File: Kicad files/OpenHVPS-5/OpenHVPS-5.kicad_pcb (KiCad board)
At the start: 2 copper layers, 40.6 x 20.8 mm, 82 parts, among them J1 Conn_01x03_Male, Q1 FQT7N10, Q2 BC846A, Q3 MMDT3906, U1 MAX6008AEUR+T, U2 74HC14, U3 MAX4162, U4 CD14538BM

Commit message: Cahnged numbering caps
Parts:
- renumbered C11 to C10, C12 to C11, C13 to C12, C14 to C13, C16 to C14, C17 to C15, C18 to C16, C20 to C17, C21 to C18, C10 to C23, C15 to C24
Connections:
- D9 pad 2: no_connect_(D9-Pad2) -> unconnected-(D9-Pad2)
- U1 pad 3: no_connect_(U1-Pad3) -> unconnected-(U1-Pad3)
- U4 pad 10: no_connect_(U4-Pad10) -> unconnected-(U4-Pad10)
- U4 pad 14: no_connect_(U4-Pad14) -> unconnected-(U4-Pad14)
- U4 pad 7: no_connect_(U4-Pad7) -> unconnected-(U4-Pad7)
- U4 pad 9: no_connect_(U4-Pad9) -> unconnected-(U4-Pad9)

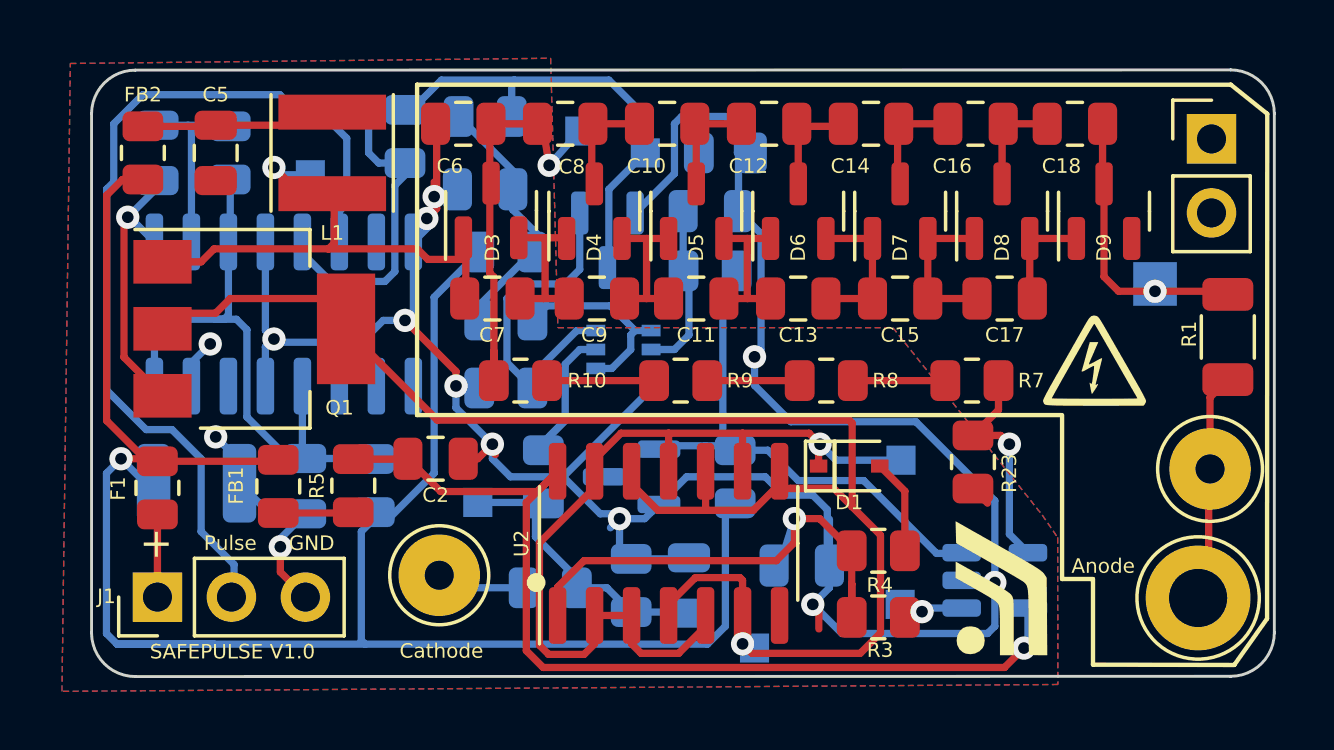
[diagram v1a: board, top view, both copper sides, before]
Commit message: fixed missing graphis and  3d model
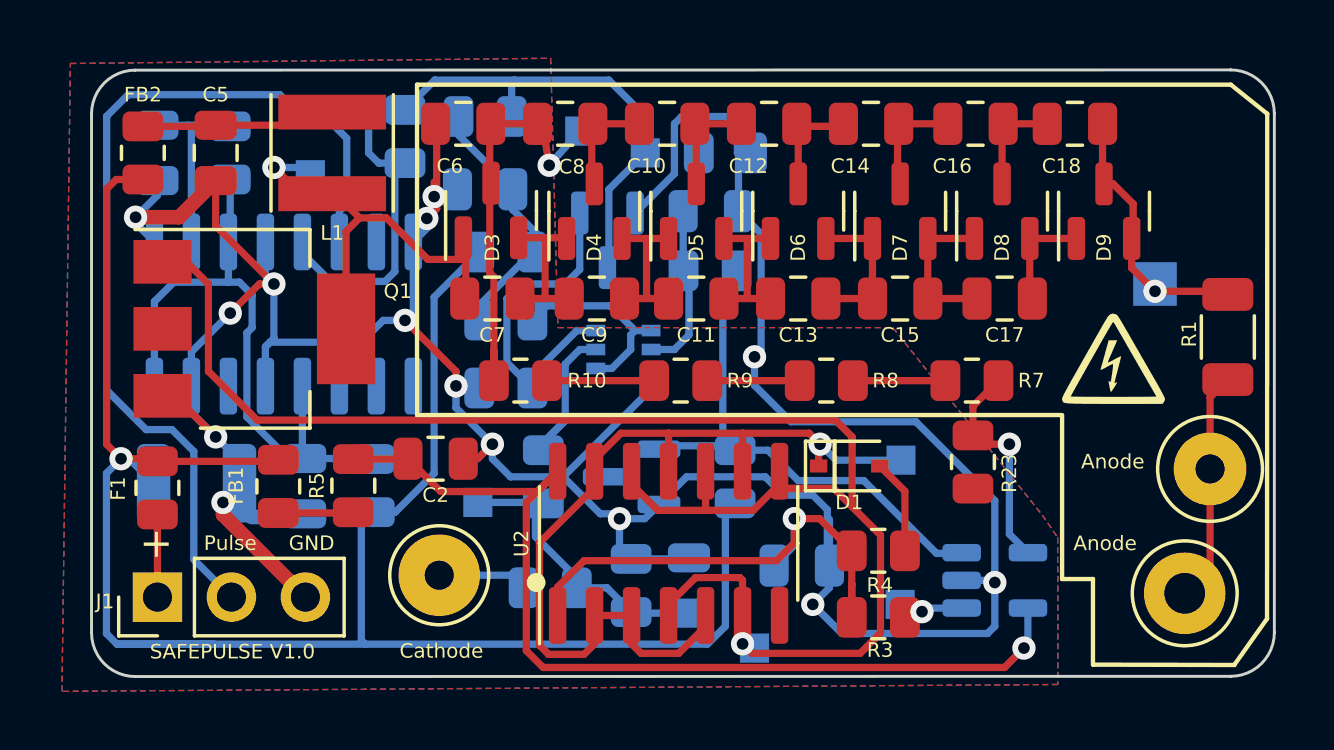
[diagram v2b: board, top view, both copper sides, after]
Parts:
- removed ?: LOGO, Symbol:QR_code_SafePulse
- removed the G*** at (157.5, 75.0)
- removed the G*** at (160.6, 67.1)
- removed the G*** at (164.5, 66.8)
- removed the H2 at (164.2, 75.3)
- removed REF**: PinHeader_1x02_P2.54mm_Vertical, Connector_PinHeader_2.54mm:PinHeader_1x02_P2.54mm_Vertical
- added G***: LOGO, Symbol:QR_code_SafePulse, F.Cu at (156.0, 64.0)
- added G2: LOGO, Symbol:HV warning, F.Cu at (161.3, 67.1)
- added G2: LOGO, Symbol:HV warning, B.Cu at (164.1, 60.2)
- added H4: Anode, TestPoint:TestPoint_Loop_D3.50mm_Drill1.4mm_Beaded, F.Cu at (163.8, 75.1)
- D3, D4, D5, D6, D7, D8, D9: value BAV23 -> BAV23S
- L1: value 2.2uH -> 4.7uH
- Q1: footprint Package_TO_SOT_SMD:SOT-223-3_TabPin2 -> Package_TO_SOT_SMD:SOT-223-3_TabPin4
- R1: value 10M -> 4.7M
- R20: value 560K -> 470K
- R4: value 100K -> 10K
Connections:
- D9 pad 2: unconnected-(D9-Pad2) -> Net-(C18-Pad2)
- Q1 pad 1: Net-(C7-Pad1) -> Net-(Q1-Pad1)
- TP4 pad 1: Net-(Q1-Pad2) -> Net-(Q1-Pad1)
- U2 pad 10: Net-(Q1-Pad2) -> Net-(Q1-Pad1)
- U2 pad 12: Net-(Q1-Pad2) -> Net-(Q1-Pad1)
- U2 pad 4: Net-(Q1-Pad2) -> Net-(Q1-Pad1)
- U2 pad 6: Net-(Q1-Pad2) -> Net-(Q1-Pad1)
- U2 pad 8: Net-(Q1-Pad2) -> Net-(Q1-Pad1)
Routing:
- net Net-(Q1-Pad1): track 0.00 -> 58.2 mm, vias 0 -> 1
- net Net-(Q1-Pad2): track 57.4 -> 0.00 mm, vias 1 -> 0
- net GND: track 117.9 -> 125.8 mm
- net Net-(C7-Pad1): track 19.3 -> 17.2 mm
- net +3V3: track 71.6 -> 70.2 mm
- net Net-(C23-Pad1): track 21.3 -> 22.5 mm
- net Net-(R3-Pad2): track 2.08 -> 1.41 mm
- net Net-(H1-Pad1): track 3.61 -> 3.08 mm
- net Net-(C18-Pad2): track 10.5 -> 9.94 mm
- net Net-(H2-Pad1): track 8.74 -> 9.25 mm

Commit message: Updated the board to V1.1.
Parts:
- removed TP7: TestPoint, TestPoint:TestPoint_Pad_1.5x1.5mm
- added two_pinheader1: Conn_01x03_Male, Connector_PinHeader_2.54mm:PinHeader_1x02_P2.54mm_Vertical, F.Cu at (165.1, 59.1)
- moved G2 7.50 mm to (164.2, 67.7)
- moved H2 2.27 mm to (162.6, 71.8)
- moved H4 1.29 mm to (162.6, 75.6)
- moved H1 1.06 mm to (138.2, 75.6)
- moved J1 0.31 mm to (128.5, 75.6)
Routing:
- net +3V3: track 70.2 -> 68.2 mm
- net Net-(C18-Pad2): vias 1 -> 0
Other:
- board text added: "SAFEPULSE V1.1"
- board text removed: "SAFEPULSE V1.0"

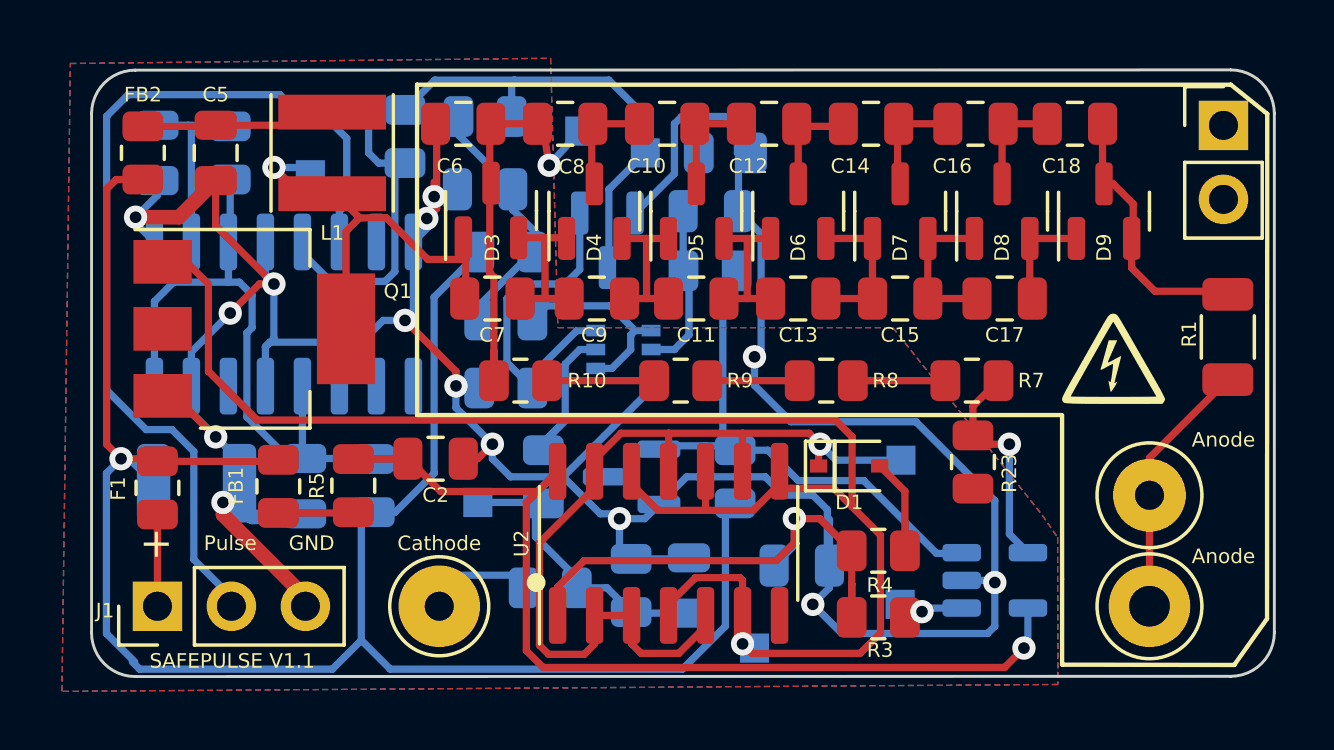
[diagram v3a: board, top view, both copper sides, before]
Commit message: Aligned more graphics and removed some via's
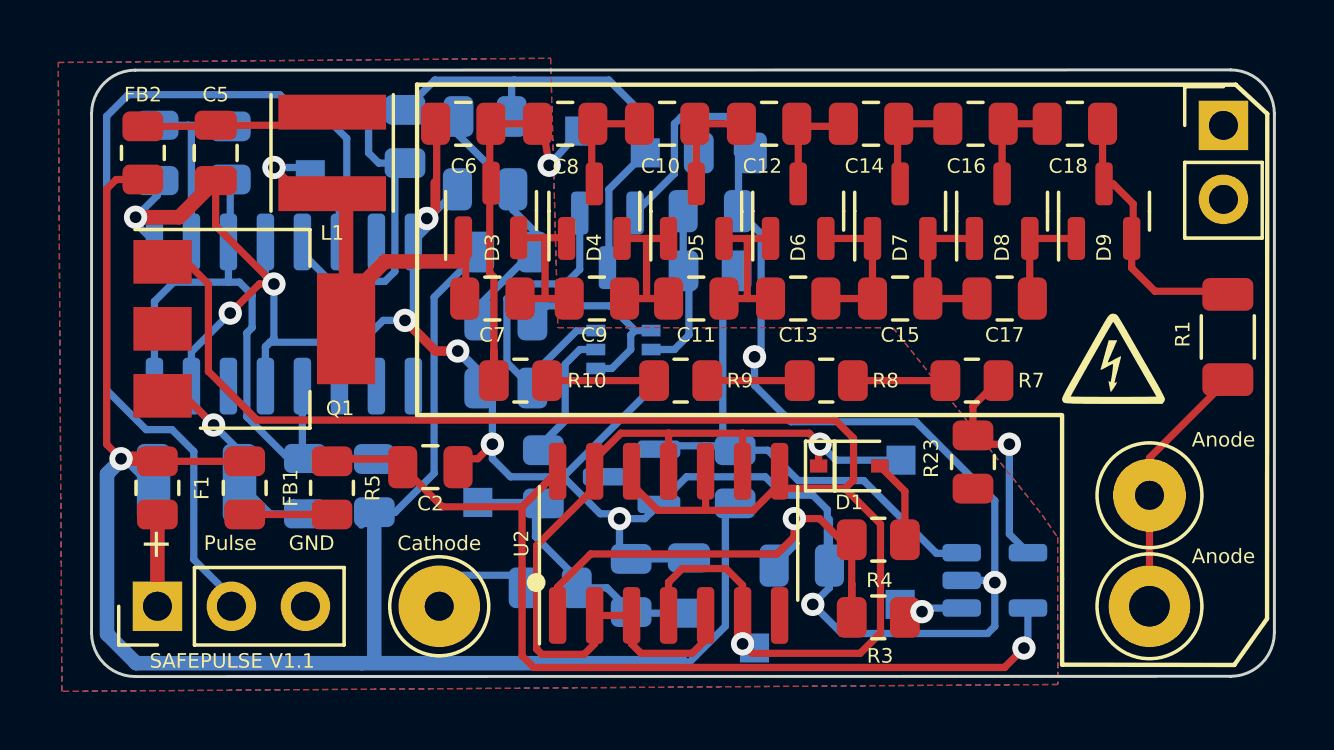
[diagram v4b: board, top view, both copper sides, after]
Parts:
- moved FB1 1.15 mm to (131.5, 71.5)
- moved R5 0.74 mm to (134.5, 71.5)
- moved R4 0.38 mm to (153.2, 73.3)
- moved C2 0.34 mm to (137.9, 70.8)
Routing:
- net Net-(C7-Pad1): track 17.2 -> 19.2 mm
- net GND: track 125.8 -> 124.4 mm, vias 14 -> 12
- net +3V3: track 68.2 -> 67.0 mm
- net Net-(Q1-Pad1): track 58.2 -> 59.4 mm

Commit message: updated board fixed via's DRC error.
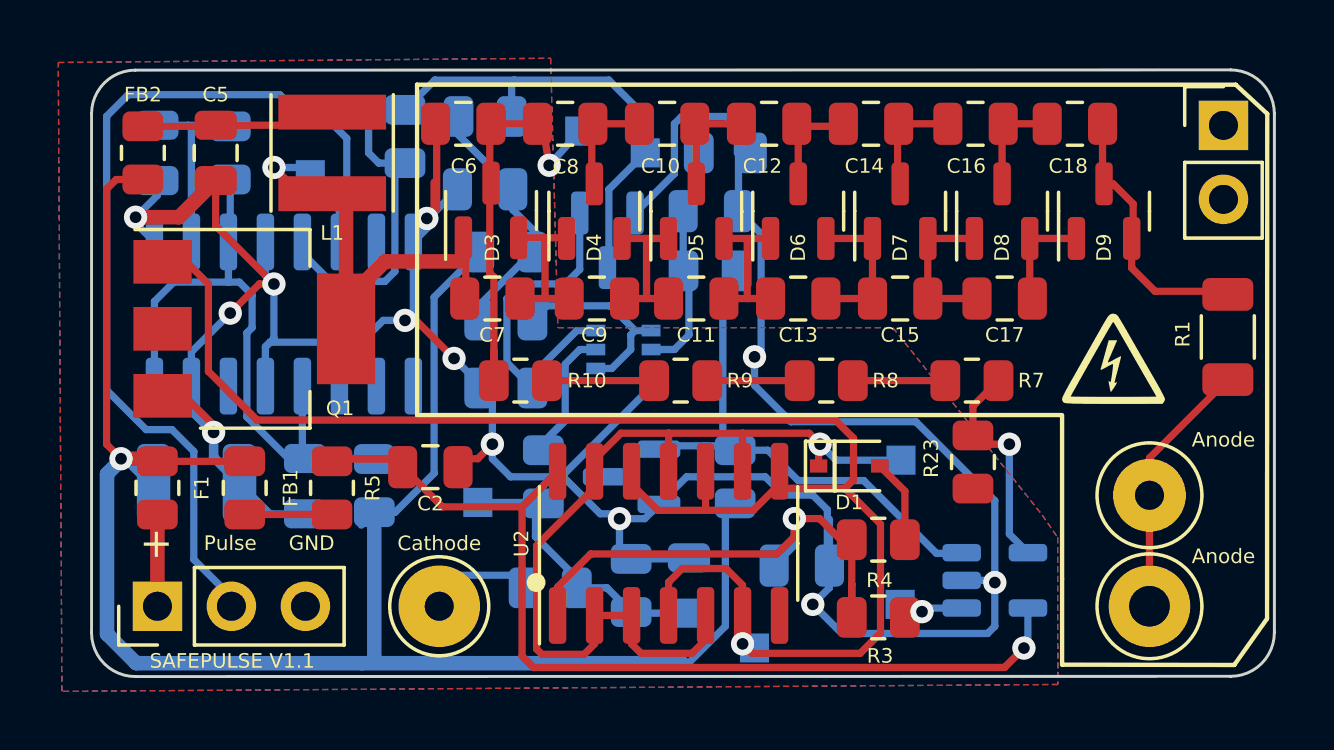
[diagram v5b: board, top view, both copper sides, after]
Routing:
- net GND: track 124.4 -> 126.5 mm
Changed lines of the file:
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@@
   (segment (start 129.242 62.208) (end 130.5 60.95) (width 0.5) (layer "F.Cu") (net 3))
   (segment (start 128.676 68.34) (end 129.09 68.34) (width 0.25) (layer "F.Cu") (net 3))
+  (segment (start 137.378 65.75) (end 138.684 67.056) (width 0.25) (layer "F.Cu") (net 3))
   (segment (start 128.676 68.34) (end 129.046 68.34) (width 0.25) (layer "F.Cu") (net 3))
   (segment (start 129.427 68.34) (end 130.429 69.342) (width 0.25) (layer "F.Cu") (net 3))
   (segment (start 127.75 62.208) (end 127.481 62.208) (width 0.25) (layer "F.Cu") (net 3))
   (segment (start 138.0875 61.9125) (end 138.0875 59) (width 0.25) (layer "F.Cu") (net 3))
-  (segment (start 138.811 66.802) (end 138.052 66.802) (width 0.3302) (layer "F.Cu") (net 3))
+  (segment (start 137 65.75) (end 137.378 65.75) (width 0.25) (layer "F.Cu") (net 3))
   (segment (start 138 62) (end 138 61) (width 0.25) (layer "F.Cu") (net 3))
-  (segment (start 138.052 66.802) (end 137 65.75) (width 0.3302) (layer "F.Cu") (net 3))
   (segment (start 137.75 62.25) (end 138 62) (width 0.25) (layer "F.Cu") (net 3))
   (segment (start 131 65.5) (end 132 64.5) (width 0.25) (layer "F.Cu") (net 3))
@@
   (via (at 132.5 64.5) (size 0.8) (drill 0.4) (layers "F.Cu" "B.Cu") (net 3))
   (via (at 127.75 62.208) (size 0.8) (drill 0.4) (layers "F.Cu" "B.Cu") (net 3))
-  (via (at 138.811 66.802) (size 0.8) (drill 0.4) (layers "F.Cu" "B.Cu") (free) (net 3))
+  (via (at 138.684 67.056) (size 0.8) (drill 0.4) (layers "F.Cu" "B.Cu") (free) (net 3))
   (via (at 157.25 74.75) (size 0.8) (drill 0.4) (layers "F.Cu" "B.Cu") (net 3))
   (via (at 131 65.5) (size 0.8) (drill 0.4) (layers "F.Cu" "B.Cu") (net 3))
@@
   (via (at 137.75 62.25) (size 0.8) (drill 0.4) (layers "F.Cu" "B.Cu") (net 3))
   (via (at 151 75.5) (size 0.8) (drill 0.4) (layers "F.Cu" "B.Cu") (net 3))
-  (via (at 130.429 69.342) (size 0.8) (drill 0.4) (layers "F.Cu" "B.Cu") (free) (net 3))
+  (via (at 130.429 69.596) (size 0.8) (drill 0.4) (layers "F.Cu" "B.Cu") (free) (net 3))
   (via (at 144.365 72.5578) (size 0.8) (layers "F.Cu" "B.Cu") (net 3))
   (via (at 137 65.75) (size 0.8) (drill 0.4) (layers "F.Cu" "B.Cu") (free) (net 3))
@@
   (segment (start 134.747 67.5418) (end 134.747 68.007) (width 0.25) (layer "B.Cu") (net 3))
   (segment (start 132.3677 66.5) (end 134.1026 66.5) (width 0.25) (layer "B.Cu") (net 3))
+  (segment (start 130.429 69.596) (end 130.429 70.4525) (width 0.3302) (layer "B.Cu") (net 3))
+  (segment (start 129.667 68.834) (end 129.667 68.007) (width 0.3302) (layer "B.Cu") (net 3))
   (segment (start 137.832 62.5121) (end 137.287 63.057) (width 0.25) (layer "B.Cu") (net 3))
+  (segment (start 130.429 69.596) (end 129.667 68.834) (width 0.3302) (layer "B.Cu") (net 3))
   (segment (start 131.318 70.568) (end 131.318 71.3415) (width 0.25) (layer "B.Cu") (net 3))
   (segment (start 127.75 62.208) (end 128.5 61.458) (width 0.25) (layer "B.Cu") (net 3))
@@
   (segment (start 148.45 62) (end 149.22502 62.77502) (width 0.25) (layer "B.Cu") (net 3))
   (segment (start 151 75.5) (end 151.572 74.928) (width 0.25) (layer "B.Cu") (net 3))
-  (segment (start 139.5495 67.5405) (end 138.811 66.802) (width 0.3302) (layer "B.Cu") (net 3))
   (segment (start 149.22502 62.77502) (end 149.22502 66.77498) (width 0.25) (layer "B.Cu") (net 3))
   (segment (start 132.207 64.207) (end 132.207 63.057) (width 0.25) (layer "B.Cu") (net 3))
@@
   (segment (start 146.668 71.12) (end 149.37 71.12) (width 0.25) (layer "B.Cu") (net 3))
   (segment (start 139.5495 68.072) (end 139.5495 67.5405) (width 0.3302) (layer "B.Cu") (net 3))
-  (segment (start 131.318 70.231) (end 130.429 69.342) (width 0.25) (layer "B.Cu") (net 3))
   (segment (start 144.365 72.5578) (end 144.365 73.5389) (width 0.25) (layer "B.Cu") (net 3))
+  (segment (start 142.433 71.12) (end 142.433 71.054728) (width 0.25) (layer "B.Cu") (net 3))
   (segment (start 146.25 60.7125) (end 146.25 59) (width 0.25) (layer "B.Cu") (net 3))
   (segment (start 134.747 68.007) (end 134.747 67.5418) (width 0.25) (layer "B.Cu") (net 3))
@@
   (segment (start 132.207 66.6607) (end 132.3677 66.5) (width 0.25) (layer "B.Cu") (net 3))
   (segment (start 151 71.75) (end 151.5 72.25) (width 0.25) (layer "B.Cu") (net 3))
-  (segment (start 130.429 69.342) (end 129.667 68.58) (width 0.25) (layer "B.Cu") (net 3))
   (segment (start 132.368 72.3915) (end 131.318 71.3415) (width 0.25) (layer "B.Cu") (net 3))
   (segment (start 134.747 67.253) (end 136.25 65.75) (width 0.25) (layer "B.Cu") (net 3))
   (segment (start 157.25 76.25) (end 157.25 74.75) (width 0.25) (layer "B.Cu") (net 3))
+  (segment (start 145.384728 68.103) (end 145.45 68.103) (width 0.25) (layer "B.Cu") (net 3))
   (segment (start 133.4615 72.5) (end 133.57 72.3915) (width 0.25) (layer "B.Cu") (net 3))
   (segment (start 144.765 73.939) (end 146.7125 73.939) (width 0.25) (layer "B.Cu") (net 3))
@@
   (segment (start 150.25 69.23) (end 149 67.98) (width 0.25) (layer "B.Cu") (net 3))
   (segment (start 132.207 66.6607) (end 132.207 68.007) (width 0.25) (layer "B.Cu") (net 3))
+  (segment (start 139.5495 68.072) (end 139.5495 67.9215) (width 0.25) (layer "B.Cu") (net 3))
   (segment (start 144.802 73.9015) (end 144.765 73.939) (width 0.25) (layer "B.Cu") (net 3))
   (segment (start 131.318 71.3415) (end 131.318 70.231) (width 0.25) (layer "B.Cu") (net 3))
@@
   (segment (start 137.8 62.25) (end 138.8 61.25) (width 0.25) (layer "B.Cu") (net 3))
   (segment (start 146.5 58.75) (end 148 58.75) (width 0.25) (layer "B.Cu") (net 3))
+  (segment (start 142.433 71.054728) (end 145.384728 68.103) (width 0.25) (layer "B.Cu") (net 3))
   (segment (start 144.365 72.5578) (end 145.23 72.5578) (width 0.25) (layer "B.Cu") (net 3))
-  (segment (start 145.45 68.103) (end 142.433 71.12) (width 0.25) (layer "B.Cu") (net 3))
   (segment (start 149.37 71.12) (end 150 71.75) (width 0.25) (layer "B.Cu") (net 3))
   (segment (start 134.747 67.1444) (end 134.747 67.5418) (width 0.25) (layer "B.Cu") (net 3))
+  (segment (start 139.5495 67.9215) (end 138.684 67.056) (width 0.25) (layer "B.Cu") (net 3))
   (segment (start 151.5 74.096) (end 151.572 74.168) (width 0.25) (layer "B.Cu") (net 3))
+  (segment (start 130.429 70.4525) (end 131.318 71.3415) (width 0.3302) (layer "B.Cu") (net 3))
   (segment (start 129.667 66.833) (end 129.667 68.007) (width 0.25) (layer "B.Cu") (net 3))
   (segment (start 140 70) (end 140 68.5225) (width 0.25) (layer "B.Cu") (net 3))
